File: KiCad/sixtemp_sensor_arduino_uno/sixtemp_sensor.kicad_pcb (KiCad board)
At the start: 2 copper layers, 53.3 x 68.6 mm, 54 parts, among them J1 Conn_Led_1, J10 debug, J12 Conn_01x12_Female, J2 Conn_Led_2, J3 Conn_Led_2, J4 Conn_Led_3, J5 Conn_Led_5, J6 Conn_Led_6, J7 I2C, J71 Temp1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

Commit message: 7 pins connectors instead of 4+3
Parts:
- removed J71: Temp1, Connector_PinSocket_2.54mm:PinSocket_1x03_P2.54mm_Vertical
- removed J72: Temp2, Connector_PinSocket_2.54mm:PinSocket_1x03_P2.54mm_Vertical
- removed J73: Temp3, Connector_PinSocket_2.54mm:PinSocket_1x03_P2.54mm_Vertical
- removed J74: Temp4, Connector_PinSocket_2.54mm:PinSocket_1x03_P2.54mm_Vertical
- removed J75: Temp5, Connector_PinSocket_2.54mm:PinSocket_1x03_P2.54mm_Vertical
- removed J76: Temp6, Connector_PinSocket_2.54mm:PinSocket_1x03_P2.54mm_Vertical
- J1: value Conn_Led_1 -> 1W/D_1; footprint Connector_PinSocket_2.54mm:PinSocket_1x04_P2.54mm_Vertical -> Connector_PinSocket_2.54mm:PinSocket_1x07_P2.54mm_Vertical
- J2: value Conn_Led_2 -> 1W/D_2; footprint Connector_PinSocket_2.54mm:PinSocket_1x04_P2.54mm_Vertical -> Connector_PinSocket_2.54mm:PinSocket_1x07_P2.54mm_Vertical
- J3: value Conn_Led_2 -> 1W/D_1; footprint Connector_PinSocket_2.54mm:PinSocket_1x04_P2.54mm_Vertical -> Connector_PinSocket_2.54mm:PinSocket_1x07_P2.54mm_Vertical
- J4: value Conn_Led_3 -> 1W/D_4; footprint Connector_PinSocket_2.54mm:PinSocket_1x04_P2.54mm_Vertical -> Connector_PinSocket_2.54mm:PinSocket_1x07_P2.54mm_Vertical
- J5: value Conn_Led_5 -> 1W/D_5; footprint Connector_PinSocket_2.54mm:PinSocket_1x04_P2.54mm_Vertical -> Connector_PinSocket_2.54mm:PinSocket_1x07_P2.54mm_Vertical
- J6: value Conn_Led_6 -> 1W/D_6; footprint Connector_PinSocket_2.54mm:PinSocket_1x04_P2.54mm_Vertical -> Connector_PinSocket_2.54mm:PinSocket_1x07_P2.54mm_Vertical
- moved J1 7.67 mm to (104.1, 40.6)
- moved J2 7.67 mm to (99.1, 40.6)
- moved J3 7.67 mm to (94.0, 40.6)
- moved J4 7.67 mm to (88.9, 40.6)
- moved J5 7.67 mm to (83.8, 40.6)
- moved J6 7.67 mm to (78.7, 40.6)
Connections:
- J1 pad 1: Net-(D1-Pad1) -> GND
- J1 pad 2: GND -> 1wire
- J1 pad 3: Net-(J1-Pad3) -> +5V
- J1 pad 4: Net-(D1-Pad2) -> Net-(D1-Pad1)
- J2 pad 1: Net-(D2-Pad1) -> GND
- J2 pad 2: GND -> 1wire
- J2 pad 3: Net-(J2-Pad3) -> +5V
- J2 pad 4: Net-(D2-Pad2) -> Net-(D2-Pad1)
- J3 pad 1: Net-(D3-Pad1) -> GND
- J3 pad 2: GND -> 1wire
- J3 pad 3: Net-(J3-Pad3) -> +5V
- J3 pad 4: Net-(D3-Pad2) -> Net-(D3-Pad1)
- J4 pad 1: Net-(D4-Pad1) -> GND
- J4 pad 2: GND -> 1wire
- J4 pad 3: Net-(J4-Pad3) -> +5V
- J4 pad 4: Net-(D4-Pad2) -> Net-(D4-Pad1)
- J5 pad 1: Net-(D5-Pad1) -> GND
- J5 pad 2: GND -> 1wire
- J5 pad 3: Net-(J5-Pad3) -> +5V
- J5 pad 4: Net-(D5-Pad2) -> Net-(D5-Pad1)
- J6 pad 1: Net-(D6-Pad1) -> GND
- J6 pad 2: GND -> 1wire
- J6 pad 3: Net-(J6-Pad3) -> +5V
- J6 pad 4: Net-(D6-Pad2) -> Net-(D6-Pad1)

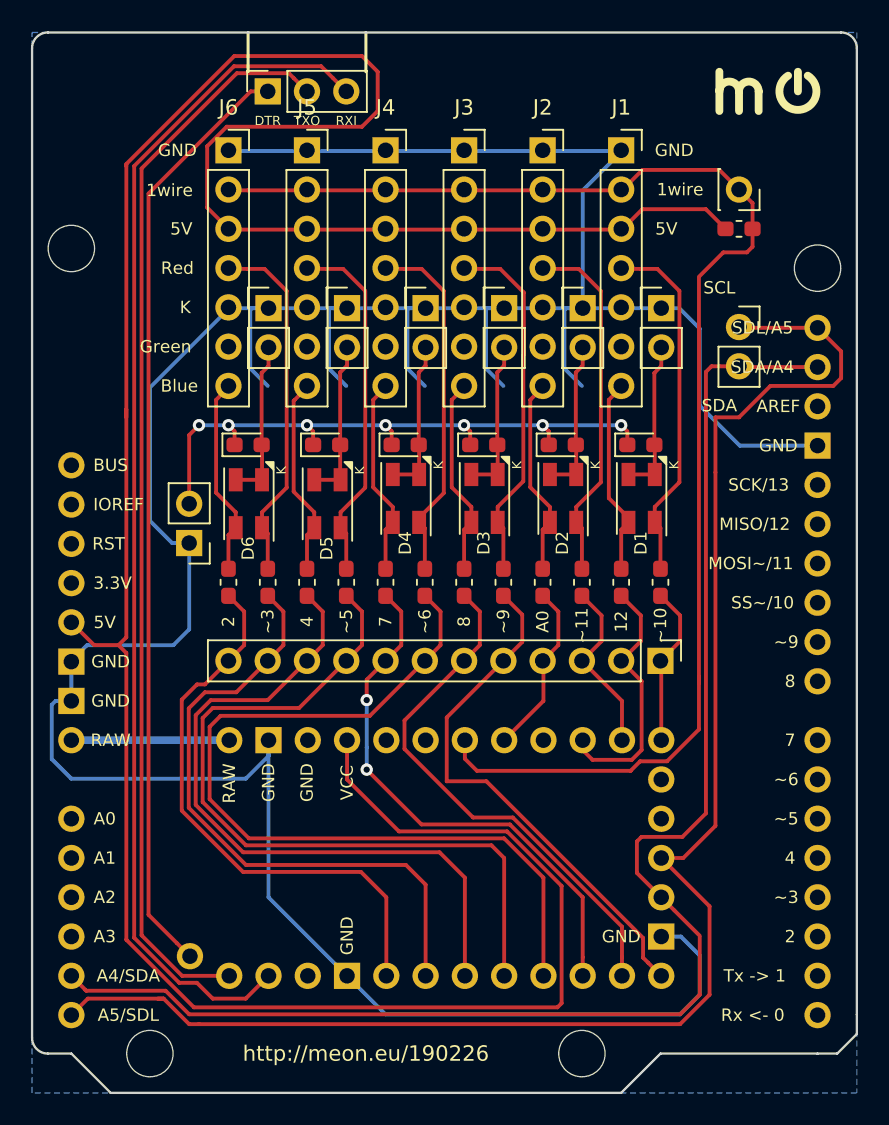
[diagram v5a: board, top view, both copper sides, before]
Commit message: uno with 2 rows, 1x12 header for direct pwm+digital pins, full 5 pin debug header
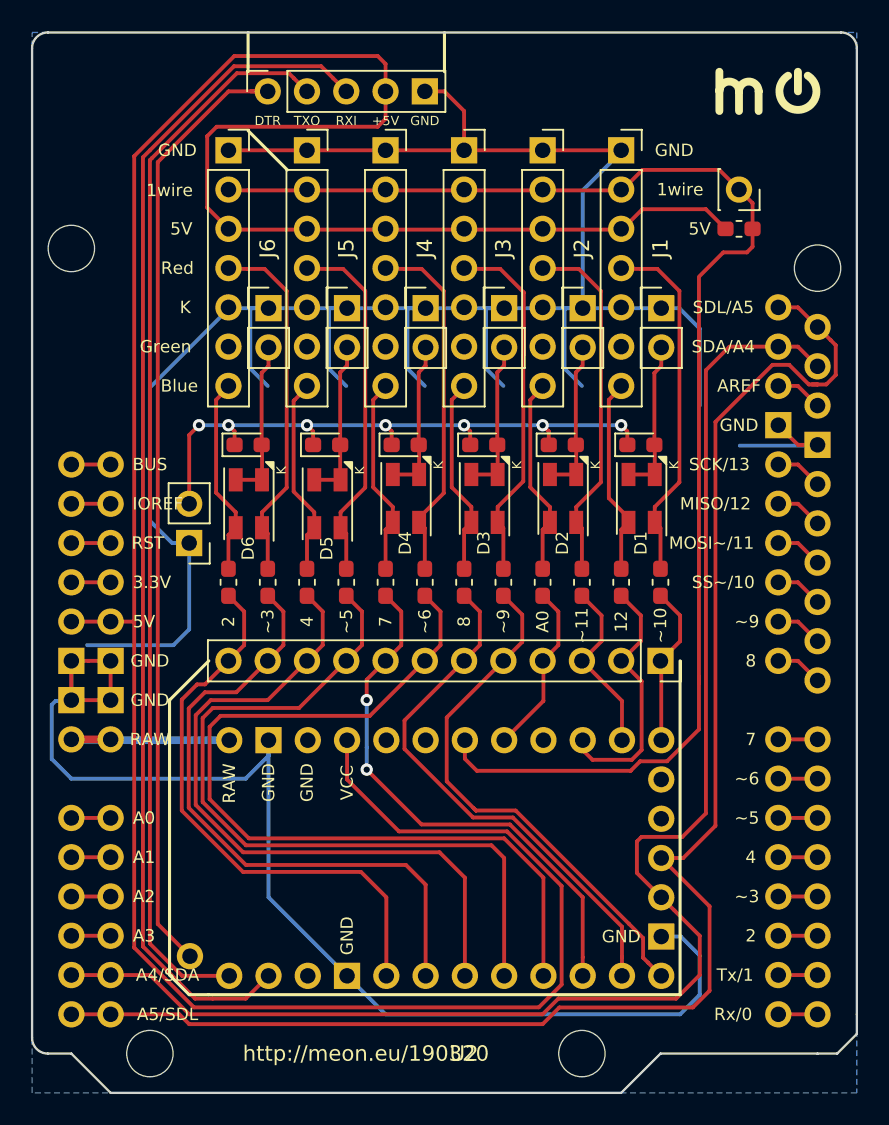
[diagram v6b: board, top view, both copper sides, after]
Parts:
- removed J7: I2C, Connector_PinSocket_2.54mm:PinSocket_1x02_P2.54mm_Vertical
- J10: footprint Connector_PinSocket_2.54mm:PinSocket_1x03_P2.54mm_Vertical -> Connector_PinSocket_2.54mm:PinSocket_1x05_P2.54mm_Vertical
- J12: footprint Connector_PinHeader_2.54mm:PinHeader_1x12_P2.54mm_Vertical -> Connector_PinSocket_2.54mm:PinSocket_1x12_P2.54mm_Vertical
- U2: footprint Arduino_Shields:Arduino_Uno_Black -> Arduino_Shields:Arduino_Uno_Black_2rows
- moved U2 0.05 mm to (94.0, 66.0)
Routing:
- net GND: track 218.3 -> 232.0 mm
- net Net-(U2-Pad15): track 0.00 -> 3.57 mm
- net Net-(U2-Pad12): track 0.00 -> 3.07 mm
- net Net-(U2-Pad20): track 0.00 -> 3.07 mm
- net Net-(U2-Pad17): track 0.00 -> 3.07 mm
- net Net-(U2-Pad16): track 0.00 -> 3.07 mm
- net Net-(U2-Pad14): track 0.00 -> 3.07 mm
- net Net-(U2-Pad13): track 0.00 -> 3.07 mm
- net RAW: track 10.2 -> 12.8 mm
- net Net-(U2-Pad96): track 0.00 -> 2.54 mm
- net Net-(U2-Pad94): track 0.00 -> 2.54 mm
- net Net-(U2-Pad90): track 0.00 -> 2.54 mm
- net Net-(U2-Pad9): track 0.00 -> 2.54 mm
- net Net-(U2-Pad32): track 0.00 -> 2.54 mm
- net Net-(U2-Pad31): track 0.00 -> 2.54 mm
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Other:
- board text added: "+5V"
- board text added: "http://meon.eu/190320"
- board text removed: "SCL"
- board text removed: "SDA"
- board text removed: "http://meon.eu/190226"

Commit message: revert physical order of light leds
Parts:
- J1: value 1W/D_1 -> 1W/D_6
- J2: value 1W/D_2 -> 1W/D_5
- J3: value 1W/D_1 -> 1W/D_4
- J4: value 1W/D_4 -> 1W/D_1
- J5: value 1W/D_5 -> 1W/D_2
- J6: value 1W/D_6 -> 1W/D_1
- moved D1 25.5 mm to (80.0, 63.5)
- moved JP1 25.5 mm to (81.3, 50.8)
- moved J1 25.4 mm to (78.7, 40.6)
- moved J6 25.4 mm to (104.1, 40.6)
- moved R11 25.4 mm to (81.3, 68.6)
- moved R12 25.4 mm to (78.7, 68.6)
- moved R61 25.4 mm to (106.7, 68.6)
- moved R62 25.4 mm to (104.1, 68.6)
- moved D19 25.4 mm to (80.0, 59.7)
- moved D69 25.4 mm to (105.4, 59.7)
- moved D6 25.4 mm to (105.4, 63.2)
- moved JP6 25.3 mm to (106.7, 50.8)
- moved JP2 15.3 mm to (86.4, 50.9)
- moved D2 15.2 mm to (85.1, 63.5)
- moved J2 15.2 mm to (83.8, 40.6)
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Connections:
- R11 pad 2: 10_~SS~~ -> D3~~
- R12 pad 2: 12_MISO -> D2
- R21 pad 2: 11_MISO~~ -> D5~~
- R22 pad 2: A0 -> D4
- R31 pad 2: D9~~ -> D6~~
- R32 pad 2: D8 -> D7
- R41 pad 2: D6~~ -> D9~~
- R42 pad 2: D7 -> D8
- R51 pad 2: D5~~ -> 11_MISO~~
- R52 pad 2: D4 -> A0
- R61 pad 2: D3~~ -> 10_~SS~~
- R62 pad 2: D2 -> 12_MISO
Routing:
- net GND: track 232.0 -> 211.3 mm

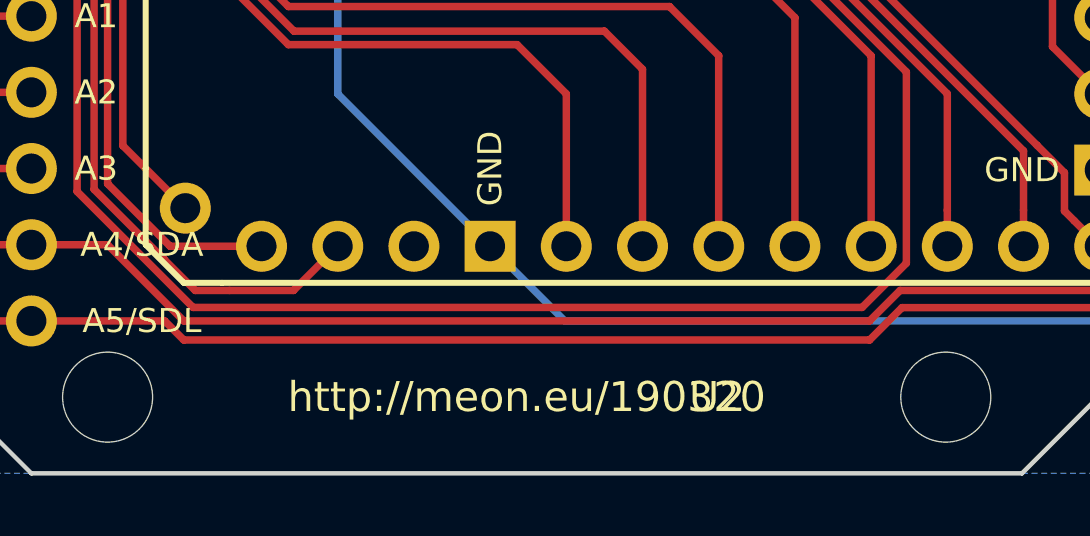
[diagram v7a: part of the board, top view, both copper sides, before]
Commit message: add 2x i2c pullups
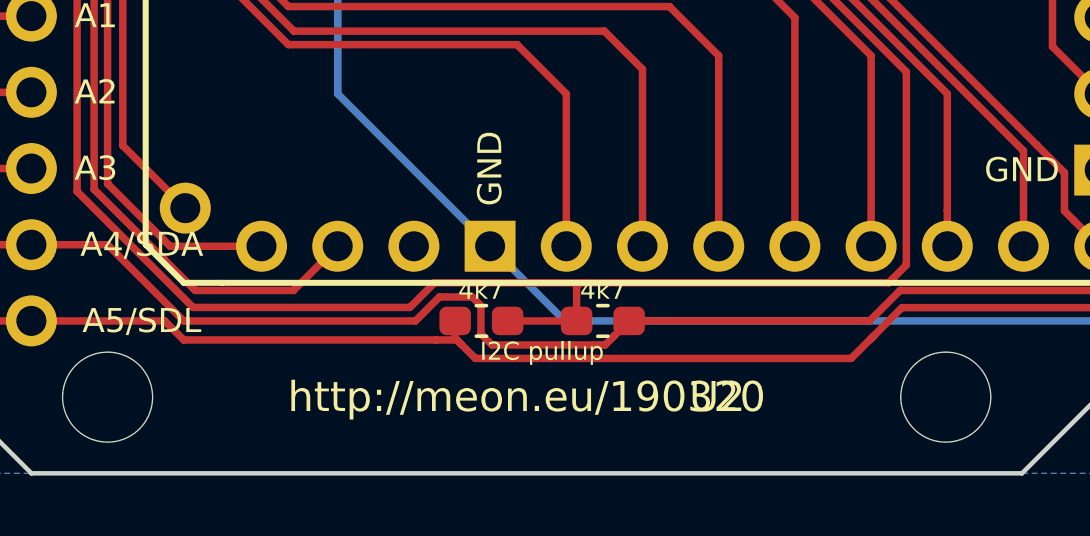
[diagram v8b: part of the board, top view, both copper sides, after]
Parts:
- added R81: 4k7, Resistor_SMD:R_0603_1608Metric_Pad1.05x0.95mm_HandSolder, F.Cu at (90.2, 96.5)
- added R82: 4k7, Resistor_SMD:R_0603_1608Metric_Pad1.05x0.95mm_HandSolder, F.Cu at (86.1, 96.5)
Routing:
- net +5V: track 185.4 -> 189.0 mm
- net SDA: track 95.3 -> 97.2 mm
- net SCL: track 99.9 -> 101.4 mm
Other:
- board text added: "I2C pullup"
